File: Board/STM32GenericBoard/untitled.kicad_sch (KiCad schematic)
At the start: 23 parts, among them J1 USB_B_Micro, J2 Conn_01x08_Pin

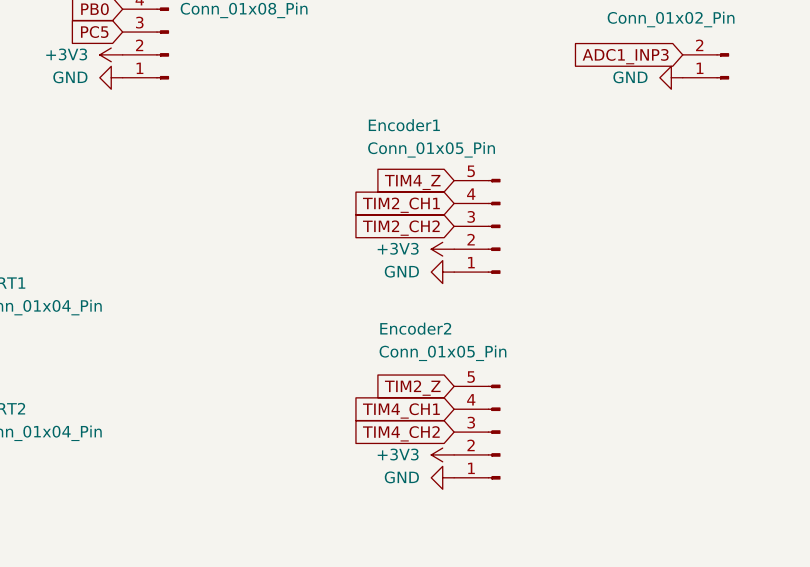
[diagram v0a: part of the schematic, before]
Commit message: feat(telemetry): add WiFi UDP bridge and UART4 DMA streaming
Add ESP32 bridge, TelemetryServer, and STM32 BalanceFrame at 200 Hz/921600.

Fix UART4 TC IRQ for HAL DMA TX completion, RPC gain tuning, and NVIC setup.

Co-authored-by: Cursor <cursoragent@cursor.com>
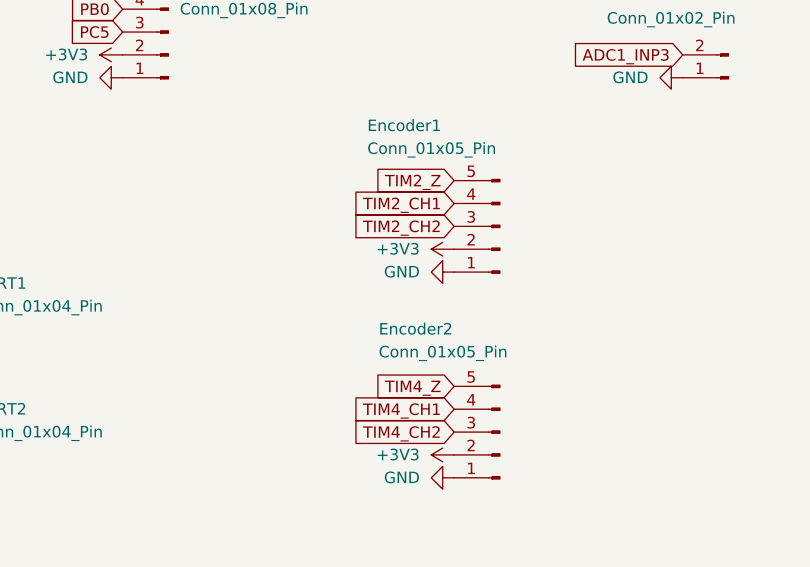
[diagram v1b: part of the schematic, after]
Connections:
- net TIM2_Z: now also Encoder1.5 (Pin_5); no longer Encoder2.5 (Pin_5)
- net TIM4_Z: now also Encoder2.5 (Pin_5); no longer Encoder1.5 (Pin_5)
